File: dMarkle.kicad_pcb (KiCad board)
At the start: 2 copper layers, 99.7 x 75 mm, 61 parts, among them SW1 SW_Choice, U1 74LS125, U10 INND-TS30RCB, U2 74HC4511, U3 Pico, U4 INND-TS30RCB, U5 74LS125, U6 74LS125, U7 74HC4511, U8 74HC4511, U9 INND-TS30RCB

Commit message: Rev 0.1
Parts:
- removed C14, C17: 0u1, Capacitor_THT:C_Rect_L4.0mm_W2.5mm_P2.50mm
- removed C18, C19: 10u, Capacitor_THT:CP_Radial_D5.0mm_P2.00mm
- removed U10, U9: INND-TS30RCB, Display_7Segment:HDSP-A151
- removed U6: 74LS125, Package_DIP:DIP-14_W7.62mm
- removed U7, U8: 74HC4511, Package_DIP:DIP-16_W7.62mm
- added D2: INND-TS30RCB, Display_7Segment:HDSP-A151, F.Cu at (152.5, 81.3)
- added D3: INND-TS30RCB, Display_7Segment:HDSP-A151, F.Cu at (160.9, 81.3)
- added D4: INND-TS30RCB, Display_7Segment:HDSP-A151, F.Cu at (169.2, 81.3)
- added Q1: 2N7000, Package_TO_SOT_THT:TO-92_Inline, F.Cu at (102.1, 87.5)
- added R29: 300, Resistor_THT:R_Axial_DIN0204_L3.6mm_D1.6mm_P5.08mm_Horizontal, F.Cu at (118.6, 91.2)
- added SW2: SW_EN, Button_Switch_THT:SW_CuK_OS102011MA1QN1_SPDT_Angled, F.Cu at (106.7, 78.7)
- C1, C3: footprint Capacitor_THT:CP_Radial_D5.0mm_P2.00mm -> Capacitor_THT:C_Rect_L4.0mm_W2.5mm_P2.50mm
- C10: value 0u1 -> 10n
- C11, C6: value 1u -> 0u1; footprint Capacitor_THT:CP_Radial_D5.0mm_P2.00mm -> Capacitor_THT:C_Rect_L4.0mm_W2.5mm_P2.50mm
- C12: value 0u1 -> 10u; footprint Capacitor_THT:C_Rect_L4.0mm_W2.5mm_P2.50mm -> Capacitor_THT:CP_Radial_D5.0mm_P2.00mm
- C13: value 1u -> 10u
- C5: value 10n -> 1u
- C7: value 0u1 -> 1u
- C8: value 10n -> 0u1
- C9: value 1u -> 10n; footprint Capacitor_THT:CP_Radial_D5.0mm_P2.00mm -> Capacitor_THT:C_Rect_L4.0mm_W2.5mm_P2.50mm
- R14: value 300 -> 330
- R7: value 330 -> 10k
- U1: value 74LS125 -> Pico; footprint Package_DIP:DIP-14_W7.62mm -> MCU_RaspberryPi_and_Boards:RPi_Pico_SMD_TH
- U3: value Pico -> 74HC4511; footprint MCU_RaspberryPi_and_Boards:RPi_Pico_SMD_TH -> Package_DIP:DIP-16_W7.62mm
- U4: value INND-TS30RCB -> 74HC4511; footprint Display_7Segment:HDSP-A151 -> Package_DIP:DIP-16_W7.62mm
- moved H4 117.7 mm to (94.0, 147.3)
- moved H2 106.8 mm to (180.8, 78.7)
- moved U4 79.3 mm to (182.9, 137.7), turned to 180 degrees
- moved U3 75.7 mm to (167.4, 137.7), turned to 180 degrees
- moved C12 65.9 mm to (95.2, 87.6), turned to 180 degrees
- moved C3 63.2 mm to (157.2, 137.7), turned to 180 degrees
- moved C6 61.4 mm to (172.7, 140.7), turned to 180 degrees
- moved C13 61.2 mm to (107.2, 87.6), turned to 0 degrees
- moved C4 60.6 mm to (157.2, 140.7), turned to 180 degrees
- moved R5 60.1 mm to (98.3, 102.9)
- moved C1 59.8 mm to (141.7, 137.7), turned to 180 degrees
- moved SW1 59.3 mm to (117.0, 129.3)
- moved U2 57.8 mm to (151.9, 137.7), turned to 180 degrees
- moved C2 57.4 mm to (141.7, 140.7), turned to 180 degrees
- moved R4 54.8 mm to (98.3, 105.4)
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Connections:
- net /D1G renamed Net-(R13-Pad1)
- C1 pad 1: +5V -> +3.3V
- C10 pad 1: +5V -> Net-(C10-Pad1)
- C11 pad 1: +5V -> Net-(C11-Pad1)
- C13 pad 1: +5V -> +3.3V
- C2 pad 1: +5V -> +3.3V
- C3 pad 1: +5V -> +3.3V
- C4 pad 1: +5V -> +3.3V
- C5 pad 1: Net-(C5-Pad1) -> +3.3V
- C6 pad 1: +5V -> +3.3V
- C7 pad 1: +5V -> +3.3V
- C8 pad 1: Net-(C8-Pad1) -> +3.3V
- C9 pad 1: +5V -> Net-(C9-Pad1)
- D1 pad 2: +5V -> +3.3V
- R1 pad 1: /R_CLK -> Net-(R1-Pad1)
- R1 pad 2: Net-(C8-Pad1) -> Net-(C10-Pad1)
- R10 pad 1: /D1D -> Net-(R10-Pad1)
- R10 pad 2: /D1Dr -> Net-(D2-Pad8)
- R11 pad 1: /D1E -> Net-(R11-Pad1)
- R11 pad 2: /D1Er -> Net-(D2-Pad9)
- R12 pad 1: /D1F -> Net-(R12-Pad1)
- R12 pad 2: /D1Fr -> Net-(D2-Pad10)
- R13 pad 2: /D1Gr -> Net-(D2-Pad3)
- R14 pad 1: Net-(D1-Pad1) -> Net-(R14-Pad1)
- R14 pad 2: GND -> Net-(D2-Pad2)
- R15 pad 1: /D2A -> Net-(U3-Pad9)
- R15 pad 2: /D2Ar -> Net-(D3-Pad4)
- R16 pad 1: /D2B -> Net-(U3-Pad10)
- R16 pad 2: /D2Br -> Net-(D3-Pad5)
- R17 pad 1: /D2C -> Net-(U3-Pad11)
- R17 pad 2: /D2Cr -> Net-(D3-Pad8)
- R18 pad 1: /D2D -> Net-(U3-Pad12)
- R18 pad 2: /D2Dr -> Net-(D3-Pad9)
- R19 pad 1: /D2E -> Net-(U3-Pad13)
- R19 pad 2: /D2Er -> Net-(D3-Pad10)
- R2 pad 1: /R_DT -> Net-(R2-Pad1)
- R2 pad 2: Net-(C5-Pad1) -> Net-(C9-Pad1)
- R20 pad 1: /D2F -> Net-(U3-Pad14)
- R20 pad 2: /D2Fr -> Net-(D3-Pad3)
- R21 pad 1: /D2G -> Net-(U3-Pad15)
- R21 pad 2: /D2Gr -> Net-(D3-Pad2)
- R22 pad 1: /D3A -> Net-(U4-Pad9)
- R22 pad 2: /D3Ar -> Net-(D4-Pad4)
- R23 pad 1: /D3B -> Net-(U4-Pad10)
- R23 pad 2: /D3Br -> Net-(D4-Pad5)
- R24 pad 1: /D3C -> Net-(U4-Pad11)
- R24 pad 2: /D3Cr -> Net-(D4-Pad8)
- R25 pad 1: /D3D -> Net-(U4-Pad12)
- R25 pad 2: /D3Dr -> Net-(D4-Pad9)
- R26 pad 1: /D3E -> Net-(U4-Pad13)
- R26 pad 2: /D3Er -> Net-(D4-Pad10)
- R27 pad 1: /D3F -> Net-(U4-Pad14)
- R27 pad 2: /D3Fr -> Net-(D4-Pad3)
- R28 pad 1: /D3G -> Net-(U4-Pad15)
- R28 pad 2: /D3Gr -> Net-(D4-Pad2)
- R3 pad 1: +3.3V -> +5V
- R3 pad 2: Net-(C5-Pad1) -> Net-(C9-Pad1)
- R4 pad 1: +3.3V -> +5V
- R4 pad 2: Net-(C8-Pad1) -> Net-(C10-Pad1)
- R5 pad 1: +3.3V -> +5V
- R6 pad 2: /R_~{SW} -> Net-(C11-Pad1)
- R7 pad 1: /D1A -> +3.3V
- R7 pad 2: /D1Ar -> GND
- R8 pad 1: /D1B -> Net-(R8-Pad1)
- R8 pad 2: /D1Br -> Net-(D2-Pad4)
- R9 pad 1: /D1C -> Net-(R9-Pad1)
- R9 pad 2: /D1Cr -> Net-(D2-Pad5)
- SW1 pad A: Net-(C8-Pad1) -> Net-(C10-Pad1)
- SW1 pad B: Net-(C5-Pad1) -> Net-(C9-Pad1)
- U1 pad 1: GND -> /D0
- U1 pad 10: GND -> /~{LE}1
- U1 pad 11: Net-(U1-Pad11) -> /~{LE}2
- U1 pad 12: /DIG0_3 -> /~{LE}3
- U1 pad 14: +5V -> unconnected-(U1-Pad14)
- U1 pad 2: /DIG0_0 -> /D1
- U1 pad 3: Net-(U1-Pad3) -> GND
- U1 pad 4: GND -> /D2
- U1 pad 5: /DIG0_1 -> /D3
- U1 pad 6: Net-(U1-Pad6) -> /~{BL}1
- U1 pad 7: GND -> /~{BL}2
- U1 pad 8: Net-(U1-Pad8) -> GND
- U1 pad 9: /DIG0_2 -> /~{BL}3
- U2 pad 1: Net-(U1-Pad6) -> /D1
- U2 pad 10: /D1D -> Net-(R9-Pad1)
- U2 pad 11: /D1C -> Net-(R10-Pad1)
- U2 pad 12: /D1B -> Net-(R11-Pad1)
- U2 pad 13: /D1A -> Net-(R12-Pad1)
- U2 pad 15: /D1F -> Net-(R14-Pad1)
- U2 pad 16: +5V -> +3.3V
- U2 pad 2: Net-(U1-Pad8) -> /D2
- U2 pad 3: +5V -> +3.3V
- U2 pad 4: +5V -> /~{BL}1
- U2 pad 5: GND -> /~{LE}1
- U2 pad 6: Net-(U1-Pad11) -> /D3
- U2 pad 7: Net-(U1-Pad3) -> /D0
- U2 pad 9: /D1E -> Net-(R8-Pad1)
- U3 pad 1: /DIG0_0 -> /D1
- U3 pad 10: /DIG1_1 -> Net-(U3-Pad10)
- U3 pad 11: /DIG1_2 -> Net-(U3-Pad11)
- U3 pad 12: /DIG1_3 -> Net-(U3-Pad12)
- U3 pad 13: GND -> Net-(U3-Pad13)
- U3 pad 14: /DIG2_0 -> Net-(U3-Pad14)
- U3 pad 15: /DIG2_1 -> Net-(U3-Pad15)
- U3 pad 16: /DIG2_2 -> +3.3V
- U3 pad 2: /DIG0_1 -> /D2
- U3 pad 3: GND -> +3.3V
- U3 pad 4: /DIG0_2 -> /~{BL}2
- U3 pad 5: /DIG0_3 -> /~{LE}2
- U3 pad 6: unconnected-(U3-Pad6) -> /D3
- U3 pad 7: unconnected-(U3-Pad7) -> /D0
- U3 pad 9: /DIG1_0 -> Net-(U3-Pad9)
- U4 pad 1: GND -> /D1
- U4 pad 10: /D1Ar -> Net-(U4-Pad10)
- U4 pad 2: /D1Fr -> /D2
- U4 pad 3: /D1Gr -> +3.3V
- U4 pad 4: /D1Er -> /~{BL}3
- U4 pad 5: /D1Dr -> /~{LE}3
- U4 pad 6: GND -> /D3
- U4 pad 7: unconnected-(U4-Pad7) -> /D0
- U4 pad 8: /D1Cr -> GND
- U4 pad 9: /D1Br -> Net-(U4-Pad9)
- U5 pad 11: Net-(U5-Pad11) -> unconnected-(U5-Pad11)
- U5 pad 12: /DIG1_3 -> unconnected-(U5-Pad12)
- U5 pad 13: GND -> unconnected-(U5-Pad13)
- U5 pad 14: +5V -> +3.3V
- U5 pad 2: /DIG1_0 -> Net-(R1-Pad1)
- U5 pad 3: Net-(U5-Pad3) -> /R_CLK
- U5 pad 5: /DIG1_1 -> Net-(R2-Pad1)
- U5 pad 6: Net-(U5-Pad6) -> /R_DT
- U5 pad 8: Net-(U5-Pad8) -> /R_~{SW}
- U5 pad 9: /DIG1_2 -> Net-(C11-Pad1)
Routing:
- net +5V: track 331.1 -> 34.2 mm
- net /D0: track 0.00 -> 199.9 mm, vias 0 -> 2
- net /D3: track 0.00 -> 176.1 mm, vias 0 -> 2
- net /D2: track 0.00 -> 146.8 mm, vias 0 -> 2
- net /D1: track 0.00 -> 144.0 mm, vias 0 -> 2
- net /D1Er: track 129.4 -> 0.00 mm, vias 3 -> 0
- net /D1Dr: track 127.8 -> 0.00 mm, vias 3 -> 0
- net /~{BL}3: track 0.00 -> 108.1 mm, vias 0 -> 1
- net /~{BL}2: track 0.00 -> 103.1 mm, vias 0 -> 2
- net /~{LE}3: track 0.00 -> 99.9 mm
- net /D1Cr: track 98.8 -> 0.00 mm, vias 3 -> 0
- net /~{LE}2: track 0.00 -> 94.9 mm, vias 0 -> 3
- net /D1Br: track 92.1 -> 0.00 mm, vias 3 -> 0
- net /~{BL}1: track 0.00 -> 90.9 mm, vias 0 -> 1
- net /D1Ar: track 85.8 -> 0.00 mm, vias 3 -> 0
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- added copper zone on F.Cu, net +3.3V
- removed copper zone on F.Cu, net GND
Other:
- board size 99.7 x 75 mm -> 97 x 78.7 mm
- rule pad_to_mask_clearance: 0.05 -> 0
- board text added: "By: Greg Coonrod Rev: 0.1"
- board text added: "DND Dice Roller"
- board text added: "JLCJLCJLCJLC"
- board text added: "Turn: Select Dice Push: Roll"
- board text added: "dMarkle"
- board text removed: "0.1uF"
- board text removed: "1uF"
- board text removed: "330Ω"
- board text removed: "Choose Your Weapon <--"
- board text removed: "ON"
- board text removed: "dMARKLE"
- board text removed: "rev 0"
- board text removed: "©Greg Coonrod"

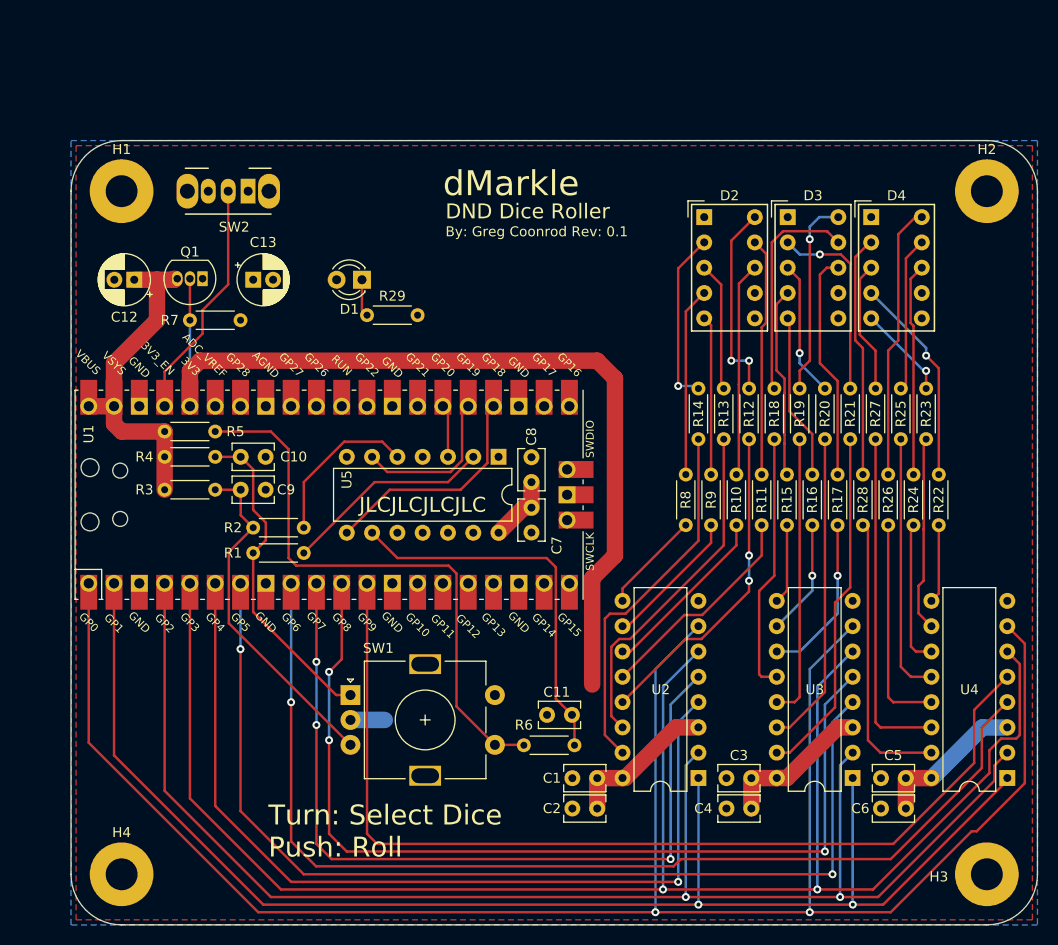
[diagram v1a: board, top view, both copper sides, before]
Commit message: All 5V usage removed. Rev0.1 complete.
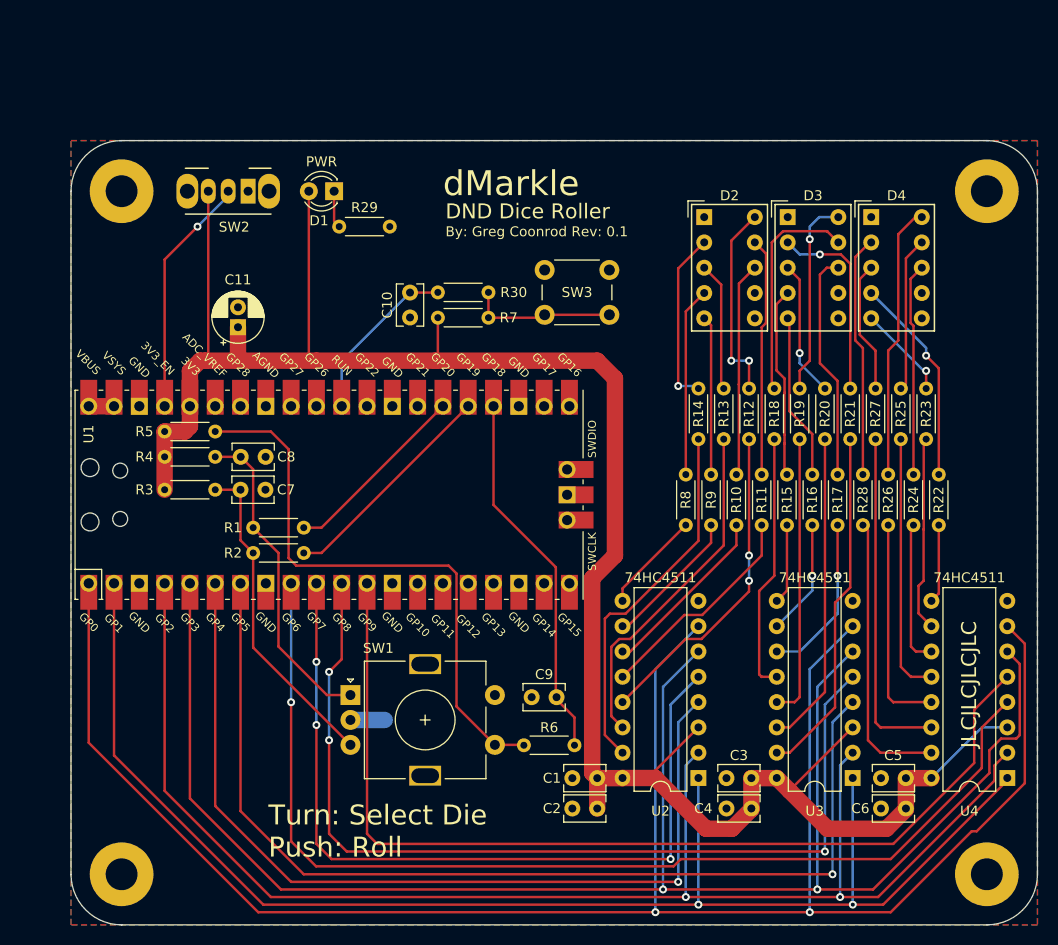
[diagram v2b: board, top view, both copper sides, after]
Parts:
- removed C12, C13: 10u, Capacitor_THT:CP_Radial_D5.0mm_P2.00mm
- removed Q1: 2N7000, Package_TO_SOT_THT:TO-92_Inline
- removed U5: 74LS125, Package_DIP:DIP-14_W7.62mm
- added R30: 200k, Resistor_THT:R_Axial_DIN0204_L3.6mm_D1.6mm_P5.08mm_Horizontal, F.Cu at (125.7, 88.9)
- added SW3: SW_RESET, Button_Switch_THT:SW_PUSH_6mm, F.Cu at (136.4, 86.7)
- C10, C9: value 10n -> 0u1
- C11: value 0u1 -> 10u; footprint Capacitor_THT:C_Rect_L4.0mm_W2.5mm_P2.50mm -> Capacitor_THT:CP_Radial_D5.0mm_P2.00mm
- C7: value 1u -> 10n
- C8: value 0u1 -> 10n
- R29: value 300 -> 330
- moved C11 51.4 mm to (105.7, 92.4), turned to 90 degrees
- moved C9 37.9 mm to (137.6, 129.5), turned to 180 degrees
- moved C8 29.3 mm to (105.9, 105.4), turned to 0 degrees
- moved C7 29.3 mm to (105.9, 108.7), turned to 0 degrees
- moved R7 24.9 mm to (125.7, 91.4)
- moved C10 23.7 mm to (122.9, 88.9), turned to -90 degrees
- moved D1 9.32 mm to (115.3, 78.7)
- moved R29 9.32 mm to (115.8, 82.3)
- moved R1 2.54 mm to (112.3, 112.5)
- moved R2 2.54 mm to (112.3, 115.1)
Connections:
- C10 pad 1: Net-(C10-Pad1) -> /~{RESET}
- C11 pad 1: Net-(C11-Pad1) -> +3.3V
- C7 pad 1: +3.3V -> Net-(C7-Pad1)
- C8 pad 1: +3.3V -> Net-(C8-Pad1)
- C9 pad 1: Net-(C9-Pad1) -> /R_~{SW}
- R1 pad 1: Net-(R1-Pad1) -> /R_CLK
- R1 pad 2: Net-(C10-Pad1) -> Net-(C8-Pad1)
- R2 pad 1: Net-(R2-Pad1) -> /R_DT
- R2 pad 2: Net-(C9-Pad1) -> Net-(C7-Pad1)
- R3 pad 1: +5V -> +3.3V
- R3 pad 2: Net-(C9-Pad1) -> Net-(C7-Pad1)
- R4 pad 1: +5V -> +3.3V
- R4 pad 2: Net-(C10-Pad1) -> Net-(C8-Pad1)
- R5 pad 1: +5V -> +3.3V
- R6 pad 2: Net-(C11-Pad1) -> /R_~{SW}
- R7 pad 2: GND -> Net-(R30-Pad2)
- SW1 pad A: Net-(C10-Pad1) -> Net-(C8-Pad1)
- SW1 pad B: Net-(C9-Pad1) -> Net-(C7-Pad1)
- U1 pad 30: unconnected-(U1-Pad30) -> /~{RESET}
- U1 pad 39: +5V -> Net-(U1-Pad39)
- U1 pad 40: +5V -> Net-(U1-Pad39)
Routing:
- net +3.3V: track 145.3 -> 215.9 mm
- net Net-(C11-Pad1): track 38.5 -> 0.00 mm
- net Net-(C9-Pad1): track 34.8 -> 0.00 mm
- net +5V: track 34.2 -> 0.00 mm
- net Net-(C10-Pad1): track 32.9 -> 0.00 mm
- net Net-(C7-Pad1): track 0.00 -> 32.7 mm
- net Net-(C8-Pad1): track 0.00 -> 32.4 mm
- net Net-(R1-Pad1): track 21.0 -> 0.00 mm
- net /~{RESET}: track 0.00 -> 17.0 mm
- net Net-(R2-Pad1): track 16.3 -> 0.00 mm
- net /R_~{SW}: track 23.0 -> 37.4 mm
- net Net-(R30-Pad2): track 0.00 -> 14.4 mm
- net /R_CLK: track 5.29 -> 19.0 mm
- net /R_DT: track 15.8 -> 22.6 mm
- net Net-(U1-Pad39): track 0.00 -> 2.54 mm
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- added copper zone on F.Cu, net GND
- removed copper zone on F.Cu, net +3.3V
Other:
- board text added: "Turn: Select Die Push: Roll"
- board text removed: "Turn: Select Dice Push: Roll"

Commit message: Readme updates and minor silkscreen changes.
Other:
- board text added: "ON"
- board text added: "Reset"
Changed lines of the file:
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@@
     (property "Sheetname" "")
     (attr through_hole)
-    (fp_text reference "SW2" (at 1.4 -3.6) (layer "F.SilkS")
+    (fp_text reference "SW2" (at 8.255 0 90) (layer "F.SilkS")
       (effects (font (size 1 1) (thickness 0.15)))
     )
@@
     (effects (font (size 1 1) (thickness 0.15)) (justify left))
   )
+  (gr_text "Reset" (at 139.7 93.345) (layer "F.SilkS")
+    (effects (font (size 1 1) (thickness 0.15)))
+  )
   (gr_text "DND Dice Roller" (at 126.492 80.772) (layer "F.SilkS")
     (effects (font (size 1.5 1.5) (thickness 0.25)) (justify left))
@@
     (effects (font (size 2 2) (thickness 0.25)) (justify left))
   )
+  (gr_text "ON" (at 102.616 82.296) (layer "F.SilkS")
+    (effects (font (size 1 1) (thickness 0.15)))
+  )
   (segment (start 107.188 115.062) (end 105.918 113.792) (width 0.25) (layer "F.Cu") (net 1))
